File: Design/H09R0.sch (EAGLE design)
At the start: 32 parts, among them P2 HEXABIT_17.32_NO_P6, P3 691311500102, U2 AD8495ARMZ-R7, U3 TLVH431ACDBVR, X1 XTALL_CSTCE8M00G52

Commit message: - Deleted old output files - Changed MCU to G0 - New schematic - New layout - Generated documentation - Generated BOM
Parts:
- removed B, C, D: PAD1, Hexabitz:PAD1
- removed C3, C4: 4.7uF, Hexabitz:C-0805-POL
- removed C5: 10nF, Hexabitz:C-0603
- removed C6: 100nF, Hexabitz:C-0603
- removed U1: (no value), Hexabitz:STM32F091CBU6
- added D2: ORANGE, HEXABITZ_USER_INTERFACE_PARTS:VLMS1300-GS08
- added D3: YELLOW, HEXABITZ_USER_INTERFACE_PARTS:VLMS1300-GS08
- added D5: BOURNS_CDSOD323-T03SCBOURNS_CDSOD323-T03SC_0_0, HEXABITZ_RCLS:BOURNS_CDSOD323-T03SCBOURNS_CDSOD323-T03SC_0_0
- added R11: 1M, Hexabitz:R-0402
- added R9: 270.0R, HEXABITZ_RCLS:R-0603
- added SWD1: (no value), pinhead:PINHD-1X3
- added U4: STM32G0B1CEU6QFN_B1CEU6_STM-L, HEXABITZ_ICs:STM32G0B1CEU6QFN_B1CEU6_STM-L
- C1: value 100nF -> 1uF; device Hexabitz:C-0603 -> HEXABITZ_RCLS:C-0805; CAPACITANCE 100nF -> (none); MFN KEMET -> (none); MPN C0603C104K8RACTU -> (none); OCTOPART_URL https://octopart.com/c0603c104k8ractu-kemet-145075?r=sp&s=9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 -> (none); TOLERANCE 10% -> (none); VOLTAGE_RATING 10V -> (none)
- C2: value 1.00uF -> 100nF; device Hexabitz:C-0805-POL -> HEXABITZ_RCLS:C-0603; CAPACITANCE 1.00uF -> (none); MFN Yageo -> (none); MPN CC0805KKX7R7BB105 -> (none); OCTOPART_URL https://octopart.com/cc0805kkx7r7bb105-yageo-8376555?r=sp&s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 -> (none); TOLERANCE 10% -> (none); VOLTAGE_RATING 16V -> (none)
- C7: device Hexabitz:C-0603 -> HEXABITZ_RCLS:C-0603; CAPACITANCE 100nF -> (none); MFN KEMET -> (none); MPN C0603C104K8RACTU -> (none); OCTOPART_URL https://octopart.com/c0603c104k8ractu-kemet-145075?r=sp&s=9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 -> (none); TOLERANCE 10% -> (none); VOLTAGE_RATING 10 -> (none)
- C8: device Hexabitz:C-0603 -> HEXABITZ_RCLS:C-0603; CAPACITANCE 100nF -> (none); MFN KEMET -> (none); MPN C0603C104K8RACTU -> (none); OCTOPART_URL https://octopart.com/c0603c104k8ractu-kemet-145075?r=sp&s=9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 -> (none); TOLERANCE 10% -> (none); VOLTAGE_RATING 10V -> (none)
- C9: value 100nF -> 4.7uF; device Hexabitz:C-0603 -> HEXABITZ_RCLS:C-0805; CAPACITANCE 100nF -> (none); MFN KEMET -> (none); MPN C0603C104K8RACTU -> (none); OCTOPART_URL https://octopart.com/c0603c104k8ractu-kemet-145075?r=sp&s=9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 -> (none); TOLERANCE 10V -> (none); VOLTAGE_RATING 10% -> (none)
- D1: value VLMS1300-GS08 -> RED; device Hexabitz:VLMS1300-GS08 -> HEXABITZ_USER_INTERFACE_PARTS:VLMS1300-GS08
- FB1: device Hexabitz:FB-TDK_MMZ1608Y300B -> HEXABITZ_RCLS:FB-0603
- P2: device Hexabitz:HEXABIT_17.32_NO_P6 -> hexabitz_connectors:HEXABIT_17.32_NO_P6
- R: value PAD1 -> R; device Hexabitz:PAD1 -> HEXABITZ_USER_INTERFACE_PARTS:PINHD-1X1
- R1: value 270.0R -> 0.0R; device Hexabitz:R-0603 -> HEXABITZ_RCLS:R-0603; MPN RC0603FR-07270RL -> RC0603JR-070RL; OCTOPART_URL https://octopart.com/search?q=RC0603FR-07270RL&start=0 -> https://octopart.com/rc0603jr-070rl-yageo-1241539?r=sp&s=X2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; RESISTANCE 270.0 Ohm -> 0.0 Ohm; TOLERANCE 1% -> (none)
- R2: value 10.0K -> 270R; device Hexabitz:R-0603 -> HEXABITZ_RCLS:R-0603; MFN Yageo -> (none); MPN RC0603JR-0710KL -> (none); OCTOPART_URL https://octopart.com/search?q=RC0603JR-0710KL&start=0 -> (none); RESISTANCE 10.0K Ohm -> (none); TOLERANCE 5% -> (none)
- R3: value 0.0R -> 10K; device Hexabitz:R-0603 -> HEXABITZ_RCLS:R-0603; MFN Yageo -> (none); MPN RC0603JR-070RL -> (none); OCTOPART_URL https://octopart.com/rc0603jr-070rl-yageo-1241539?r=sp&s=X2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 -> (none); RESISTANCE 0.0 Ohm -> (none)
- R8: value 1M -> 270.0R; device Hexabitz:R-0402 -> HEXABITZ_RCLS:R-0603; MFN Yageo -> (none); MPN RC0402FR-071ML -> (none); OCTOPART_URL https://octopart.com/search?q=RC0402FR-071ML&start=0 -> (none); RESISTANCE 1M -> (none); TOLERANCE 1% -> (none)
- X1: device Hexabitz:XTALL_CSTCE8M00G52 -> HEXABITZ_RCLS:XTALL_CSTCE8M00G52
- renumbered P3 to JP1
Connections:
- removed net B: B.P$1, R2.2, U1.PF11-OSC_BOOT0
- removed net N$1: D.P$1, U1.PA13
- removed net N$2: C.P$1, U1.PA14
- removed net R: C1.1, R.P$1, U1.NRST
- removed net USART1_RX: P2.SD5, U1.PA10
- removed net USART1_TX: P2.SU5, U1.PA9
- new net CLK: R3.2, SWD1.1, SWD1.2, U4.PA14-BOOT0
- new net DATA: SWD1.3, U4.PA13
- new net N$16: D1.A, R2.2
- new net N$17: R8.2, U4.PB5
- new net N$18: R9.2, U4.PB4
- new net N$19: D2.A, R9.1
- new net N$20: D3.A, R8.1
- new net USART5_RX: P2.SD4, U4.PB1
- new net USART5_TX: P2.SU4, U4.PB0
- net GND: now also C2.2, D2.C, D3.C, D5.A, R1.1, R11.1, U4.VSS; no longer C1.2, C3.-, C4.-, C6.2, C7.2, C8.2, C9.2, R2.1, R8.1, U1.EP, U1.VSS_0, U1.VSS_1, U1.VSS_2
- net N$10: now also U4.PF0-OSC_IN, X1.3; no longer D1.A, R1.1
- net N$14: now also C2.1, R.1, U4.PF2-NRST; no longer U1.PF0-OSC_IN, X1.1
- net N$15: now also R2.1, U4.PA6; no longer U1.PF1-OSC_OUT, X1.3
- net N$8: now also U4.PF1-OSC_OUT, X1.1; no longer R1.2, U1.PA11
- net TEMP1: no longer U1.PA7
- net TYPE_K_THC_IN-: now also R11.2; no longer R8.2
- net USART2_RX: now also P2.SD3, U4.PA3; no longer P2.SD2, U1.PA3
- net USART2_TX: now also P2.SU3, U4.PA2; no longer P2.SU2, U1.PA2
- net USART3_RX: now also P2.SD5, U4.PB11; no longer P2.SD4, U1.PB11
- net USART3_TX: now also P2.SU5, U4.PB10; no longer P2.SU4, U1.PB10
- net USART4_RX: now also P2.SD2, U4.PA1; no longer P2.SD1, U1.PA1
- net USART4_TX: now also P2.SU2, U4.PA0; no longer P2.SU1, U1.PA0
- net USART6_RX: now also P2.SD1, U4.PB9; no longer P2.SD3, U1.PA5
- net USART6_TX: now also P2.SU1, U4.PB8; no longer P2.SU3, U1.PA4
- net VDD: now also D5.C, P2.VDD1, P2.VDD2, P2.VDD3, P2.VDD4, P2.VDD5, P2.VDD6; no longer C3.+, C4.+, C6.1, C7.1, C8.1, C9.1, P2.VCC1, P2.VCC2, P2.VCC3, P2.VCC4, P2.VCC5, P2.VCC6, U1.VBAT, U1.VDDIO2, U1.VDD_0, U1.VDD_1
- net VDDA: now also C1.1, C7.1, C8.1, C9.1, U4.VBAT, U4.VDD/VDDA, U4.VREF+; no longer C2.+, C5.1, U1.VDDA
- net VSSA: now also C1.2, C7.2, C8.2, C9.2, R1.2, U4.VSS/VSSA; no longer C2.-, C5.2, R3.2, U1.VSS_A
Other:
- note added: "BOOT"
- note added: "H09R01_Backend"
- note added: "H09R01_Frontend"
- note added: "VDD\VDDA Coupling"
- note added: "Vref Coupling"
- note removed: "0"
- note removed: "H09R0_Backend"
- note removed: "H09R0_Frontend"
- note removed: "VBAT"
- note removed: "VDD Coupling"
- note removed: "VDDA Coupling"
- note removed: "VDDIO2 Coupling"
- moved on the sheet: C1, C7, C8, C9, D1, FB1, R1, R2, R3, X1

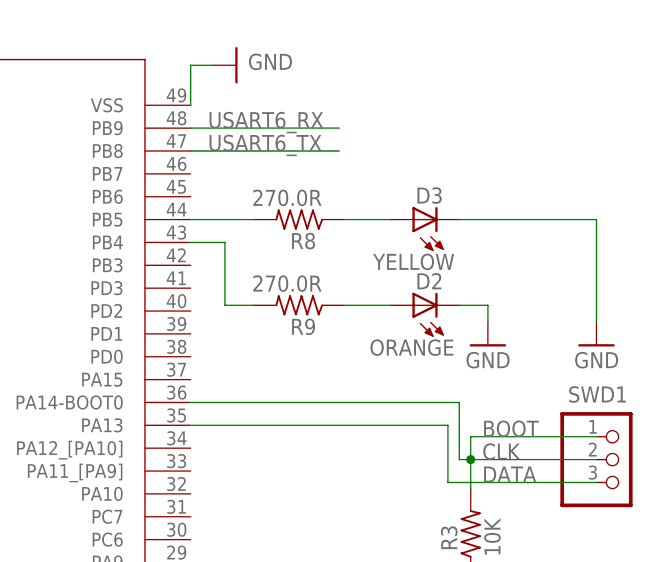
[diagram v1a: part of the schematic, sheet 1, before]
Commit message: - Deleted yellow and orange LEDs from design - Changed connector - Changed RESs and CAPs and used from our library - New layout - Changed polygon to thermal - Rearranged compenents in BOM
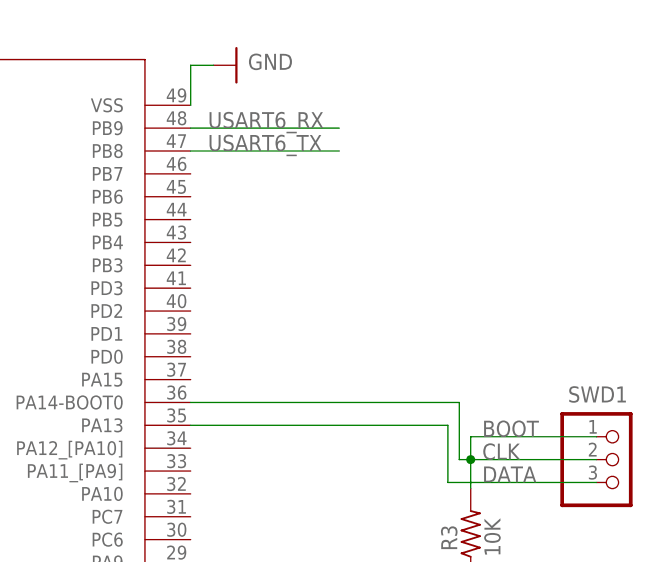
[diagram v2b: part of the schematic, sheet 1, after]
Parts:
- removed D2: ORANGE, HEXABITZ_USER_INTERFACE_PARTS:VLMS1300-GS08
- removed D3: YELLOW, HEXABITZ_USER_INTERFACE_PARTS:VLMS1300-GS08
- removed R8, R9: 270.0R, HEXABITZ_RCLS:R-0603
- C10, C12, C13, C14: device Hexabitz:C-0603 -> HEXABITZ_RCLS:C-0603
- JP1: device Hexabitz:691311500102 -> HEXABITZ_CONNECTION_PARTS:1546111-2
- R11, R4, R5, R6: device Hexabitz:R-0402 -> HEXABITZ_RCLS:R-0402
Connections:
- removed net N$17: R8.2, U4.PB5
- removed net N$18: R9.2, U4.PB4
- removed net N$19: D2.A, R9.1
- removed net N$20: D3.A, R8.1
- net GND: no longer D2.C, D3.C
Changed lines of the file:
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@@
 <part name="GND4" library="supply1" deviceset="GND" device=""/>
 <part name="P2" library="hexabitz_connectors" library_urn="urn:adsk.eagle:library:20064578" deviceset="HEXABIT_?_NO_P6" device="17.32" package3d_urn="urn:adsk.eagle:package:20064635/2"/>
-<part name="R11" library="Hexabitz" deviceset="R-0402" device="" value="1M">
+<part name="R11" library="HEXABITZ_RCLS" library_urn="urn:adsk.eagle:library:20064561" deviceset="R-0402" device="" package3d_urn="urn:adsk.eagle:package:19666455/3" value="1M">
 <attribute name="MFN" value="Yageo"/>
 <attribute name="MPN" value="RC0402FR-071ML"/>
@@
 <part name="GND16" library="supply1" deviceset="GND" device=""/>
 <part name="U3" library="Hexabitz" deviceset="TLVH431ACDBVR" device=""/>
-<part name="C13" library="Hexabitz" deviceset="C-0603" device="" value="10nF">
+<part name="C13" library="HEXABITZ_RCLS" library_urn="urn:adsk.eagle:library:20064561" deviceset="C-0603" device="" package3d_urn="urn:adsk.eagle:package:19666468/3" value="10nF">
 <attribute name="CAPACITANCE" value="10nF"/>
 <attribute name="MFN" value="KEMET"/>
@@
 <attribute name="VOLTAGE_RATING" value="50V"/>
 </part>
-<part name="C12" library="Hexabitz" deviceset="C-0603" device="" value="100nF">
+<part name="C12" library="HEXABITZ_RCLS" library_urn="urn:adsk.eagle:library:20064561" deviceset="C-0603" device="" package3d_urn="urn:adsk.eagle:package:19666468/3" value="100nF">
 <attribute name="CAPACITANCE" value="100nF"/>
 <attribute name="MFN" value="KEMET"/>
@@
 <part name="SUPPLY1" library="supply2" deviceset="VDD" device=""/>
 <part name="GND17" library="supply1" deviceset="GND" device=""/>
-<part name="JP1" library="Hexabitz" deviceset="691311500102" device="" value="691311500102"/>
-<part name="C14" library="Hexabitz" deviceset="C-0603" device="" value="100nF">
+<part name="JP1" library="HEXABITZ_CONNECTION_PARTS" library_urn="urn:adsk.eagle:library:20064553" deviceset="1546111-2" device="" package3d_urn="urn:adsk.eagle:package:19666461/4" value="691311500102"/>
+<part name="C14" library="HEXABITZ_RCLS" library_urn="urn:adsk.eagle:library:20064561" deviceset="C-0603" device="" package3d_urn="urn:adsk.eagle:package:19666468/3" value="100nF">
 <attribute name="CAPACITANCE" value="100nF"/>
 <attribute name="MFN" value="KEMET"/>
@@
 <attribute name="VOLTAGE_RATING" value="10V"/>
 </part>
-<part name="R4" library="Hexabitz" deviceset="R-0402" device="" value="1k">
+<part name="R4" library="HEXABITZ_RCLS" library_urn="urn:adsk.eagle:library:20064561" deviceset="R-0402" device="" package3d_urn="urn:adsk.eagle:package:19666455/3" value="1k">
 <attribute name="MFN" value="Yageo"/>
 <attribute name="MPN" value="RC0402FR-071KL"/>
@@
 <attribute name="TOLERANCE" value="1%"/>
 </part>
-<part name="R5" library="Hexabitz" deviceset="R-0402" device="" value="100">
+<part name="R5" library="HEXABITZ_RCLS" library_urn="urn:adsk.eagle:library:20064561" deviceset="R-0402" device="" package3d_urn="urn:adsk.eagle:package:19666455/3" value="100">
 <attribute name="MFN" value="Yageo"/>
 <attribute name="MPN" value="RC0402FR-07100RL"/>
@@
 <attribute name="TOLERANCE" value="1%"/>
 </part>
-<part name="R6" library="Hexabitz" deviceset="R-0402" device="" value="100">
+<part name="R6" library="HEXABITZ_RCLS" library_urn="urn:adsk.eagle:library:20064561" deviceset="R-0402" device="" package3d_urn="urn:adsk.eagle:package:19666455/3" value="100">
 <attribute name="MFN" value="Yageo"/>
 <attribute name="MPN" value="RC0402FR-07100RL"/>
@@
 <attribute name="TOLERANCE" value="1%"/>
 </part>
-<part name="C10" library="Hexabitz" deviceset="C-0603" device="" value="10nF">
+<part name="C10" library="HEXABITZ_RCLS" library_urn="urn:adsk.eagle:library:20064561" deviceset="C-0603" device="" package3d_urn="urn:adsk.eagle:package:19666468/3" value="10nF">
 <attribute name="CAPACITANCE" value="10nF"/>
 <attribute name="MFN" value="KEMET"/>
@@
 <part name="SUPPLY18" library="HEXABITZ_CONNECTION_PARTS" library_urn="urn:adsk.eagle:library:20064553" deviceset="VSSA" device=""/>
 <part name="D5" library="HEXABITZ_RCLS" library_urn="urn:adsk.eagle:library:20064561" deviceset="BOURNS_CDSOD323-T03SC" device="BOURNS_CDSOD323-T03SC_0_0" package3d_urn="urn:adsk.eagle:package:20526306/2"/>
-<part name="R8" library="HEXABITZ_RCLS" library_urn="urn:adsk.eagle:library:20064561" deviceset="R-0603" device="" package3d_urn="urn:adsk.eagle:package:1435818/6" value="270.0R"/>
-<part name="R9" library="HEXABITZ_RCLS" library_urn="urn:adsk.eagle:library:20064561" deviceset="R-0603" device="" package3d_urn="urn:adsk.eagle:package:1435818/6" value="270.0R"/>
-<part name="GND22" library="supply1" library_urn="urn:adsk.eagle:library:371" deviceset="GND" device=""/>
-<part name="GND23" library="supply1" library_urn="urn:adsk.eagle:library:371" deviceset="GND" device=""/>
-<part name="D3" library="HEXABITZ_USER_INTERFACE_PARTS" library_urn="urn:adsk.eagle:library:20064563" deviceset="VLMS1300-GS08" device="" package3d_urn="urn:adsk.eagle:package:20064571/3" value="YELLOW">
-<attribute name="OCTOPART_URL" value="https://octopart.com/vlms1300-gs08-vishay-21709201?r=sp&amp;s=_gcP4_q8T1SC6PJQPTQ9yA"/>
-</part>
-<part name="D2" library="HEXABITZ_USER_INTERFACE_PARTS" library_urn="urn:adsk.eagle:library:20064563" deviceset="VLMS1300-GS08" device="" package3d_urn="urn:adsk.eagle:package:20064571/3" value="ORANGE">
-<attribute name="OCTOPART_URL" value="https://octopart.com/vlms1300-gs08-vishay-21709201?r=sp&amp;s=_gcP4_q8T1SC6PJQPTQ9yA"/>
-</part>
 </parts>
 <sheets>
@@
 <attribute name="NAME" x="131.2084" y="86.0436" size="1.778" layer="95" rot="R90"/>
 </instance>
-<instance part="R8" gate="G$1" x="229.735" y="173.445" smashed="yes" rot="R180">
-<attribute name="NAME" x="231.64" y="171.9464" size="1.778" layer="95" rot="R180"/>
-<attribute name="VALUE" x="232.275" y="176.747" size="1.778" layer="96" rot="R180"/>
-</instance>
-<instance part="R9" gate="G$1" x="229.735" y="163.92" smashed="yes" rot="R180">
-<attribute name="NAME" x="231.64" y="162.4214" size="1.778" layer="95" rot="R180"/>
-<attribute name="VALUE" x="232.275" y="167.222" size="1.778" layer="96" rot="R180"/>
-</instance>
-<instance part="GND22" gate="1" x="250.69" y="159.475" smashed="yes" rot="MR0">
-<attribute name="VALUE" x="253.23" y="156.935" size="1.778" layer="96" rot="MR0"/>
-</instance>
-<instance part="GND23" gate="1" x="262.755" y="159.475" smashed="yes" rot="MR0">
-<attribute name="VALUE" x="265.295" y="156.935" size="1.778" layer="96" rot="MR0"/>
-</instance>
-<instance part="D3" gate="G$1" x="242.435" y="173.445" smashed="yes" rot="R180">
-<attribute name="NAME" x="245.737" y="177.001" size="1.778" layer="95" rot="R180"/>
-<attribute name="VALUE" x="247.007" y="169.635" size="1.778" layer="96" rot="R180"/>
-</instance>
-<instance part="D2" gate="G$1" x="242.435" y="163.92" smashed="yes" rot="R180">
-<attribute name="NAME" x="245.737" y="167.476" size="1.778" layer="95" rot="R180"/>
-<attribute name="VALUE" x="247.007" y="160.11" size="1.778" layer="96" rot="R180"/>
-</instance>
 </instances>
 <busses>
@@
 <wire x1="121.15" y1="120.105" x2="121.15" y2="122.645" width="0.1524" layer="91"/>
 </segment>
-<segment>
-<pinref part="GND22" gate="1" pin="GND"/>
-<wire x1="250.69" y1="162.015" x2="250.69" y2="163.92" width="0.1524" layer="91"/>
-<wire x1="250.69" y1="163.92" x2="247.515" y2="163.92" width="0.1524" layer="91"/>
-<pinref part="D2" gate="G$1" pin="C"/>
-</segment>
-<segment>
-<pinref part="GND23" gate="1" pin="GND"/>
-<wire x1="247.515" y1="173.445" x2="262.755" y2="173.445" width="0.1524" layer="91"/>
-<wire x1="262.755" y1="173.445" x2="262.755" y2="162.015" width="0.1524" layer="91"/>
-<pinref part="D3" gate="G$1" pin="C"/>
-</segment>
 </net>
 <net name="USART3_TX" class="0">
@@
 </segment>
 </net>
-<net name="N$17" class="0">
-<segment>
-<pinref part="U4" gate="A" pin="PB5"/>
-<pinref part="R8" gate="G$1" pin="2"/>
-<wire x1="217.67" y1="173.445" x2="224.655" y2="173.445" width="0.1524" layer="91"/>
-</segment>
-</net>
-<net name="N$18" class="0">
-<segment>
-<pinref part="U4" gate="A" pin="PB4"/>
-<wire x1="217.67" y1="170.905" x2="221.48" y2="170.905" width="0.1524" layer="91"/>
-<wire x1="221.48" y1="170.905" x2="221.48" y2="163.92" width="0.1524" layer="91"/>
-<pinref part="R9" gate="G$1" pin="2"/>
-<wire x1="221.48" y1="163.92" x2="224.655" y2="163.92" width="0.1524" layer="91"/>
-</segment>
-</net>
-<net name="N$19" class="0">
-<segment>
-<pinref part="R9" gate="G$1" pin="1"/>
-<wire x1="234.815" y1="163.92" x2="239.895" y2="163.92" width="0.1524" layer="91"/>
-<pinref part="D2" gate="G$1" pin="A"/>
-</segment>
-</net>
-<net name="N$20" class="0">
-<segment>
-<pinref part="R8" gate="G$1" pin="1"/>
-<wire x1="234.815" y1="173.445" x2="239.895" y2="173.445" width="0.1524" layer="91"/>
-<pinref part="D3" gate="G$1" pin="A"/>
-</segment>
-</net>
